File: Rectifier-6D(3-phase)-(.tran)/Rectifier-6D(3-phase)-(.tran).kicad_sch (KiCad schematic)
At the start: 11 parts

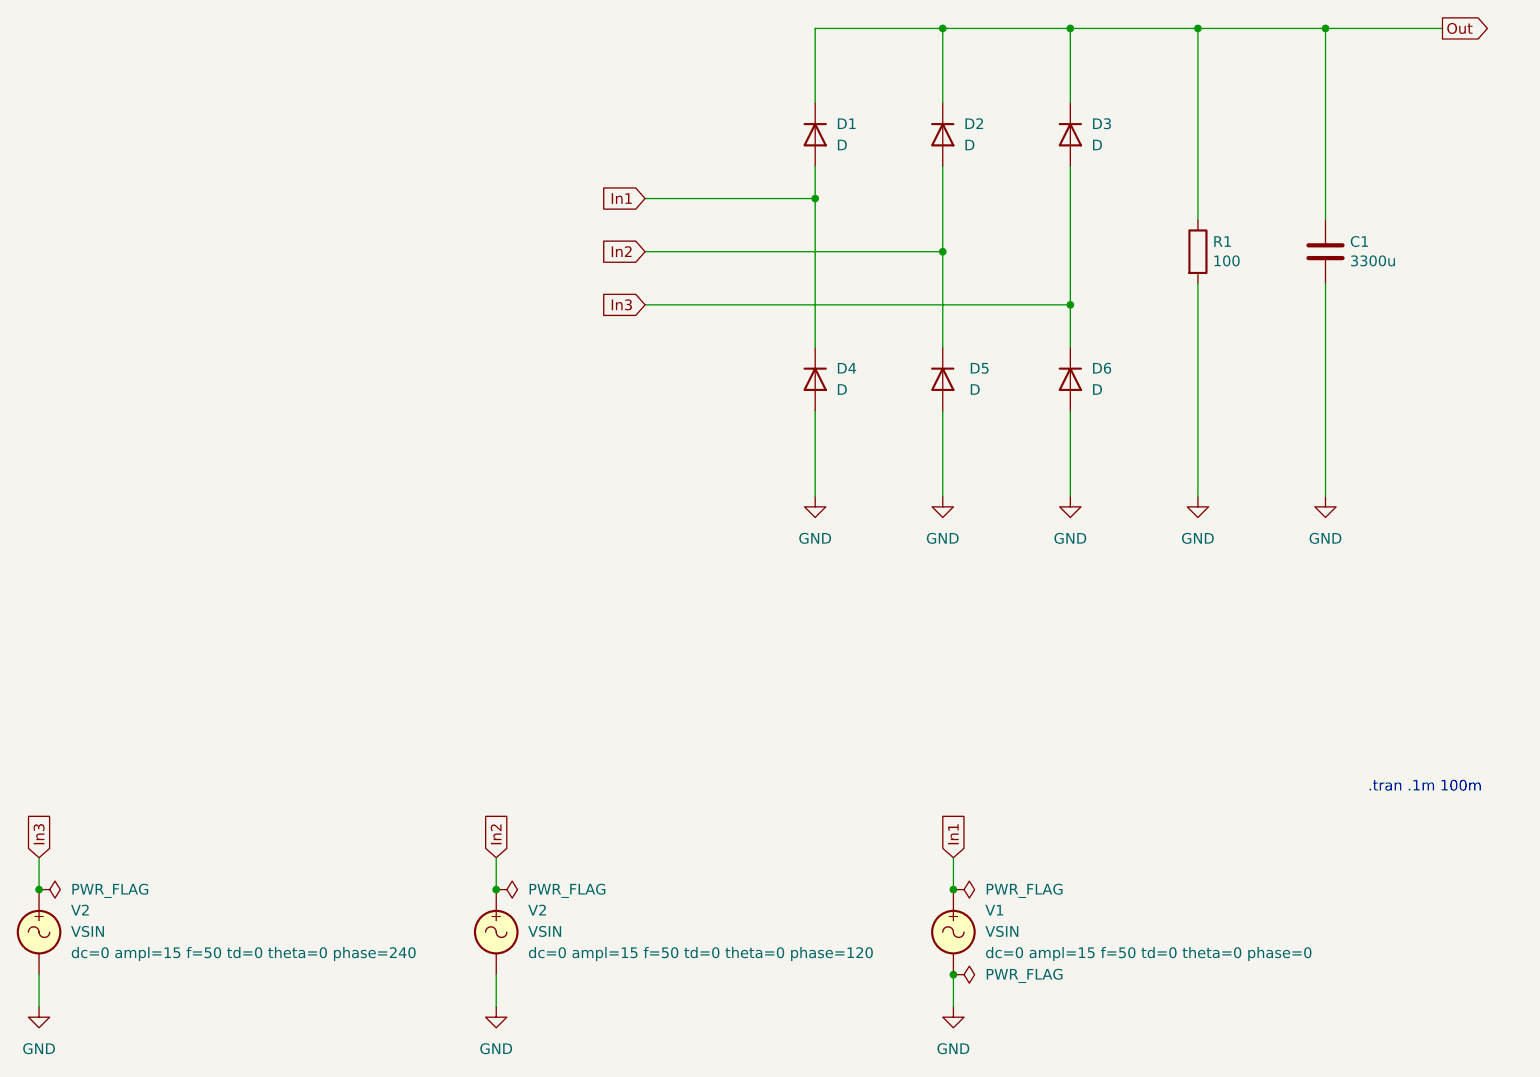
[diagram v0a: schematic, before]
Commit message: Updated all schematics and prepared for KiCad 8.0
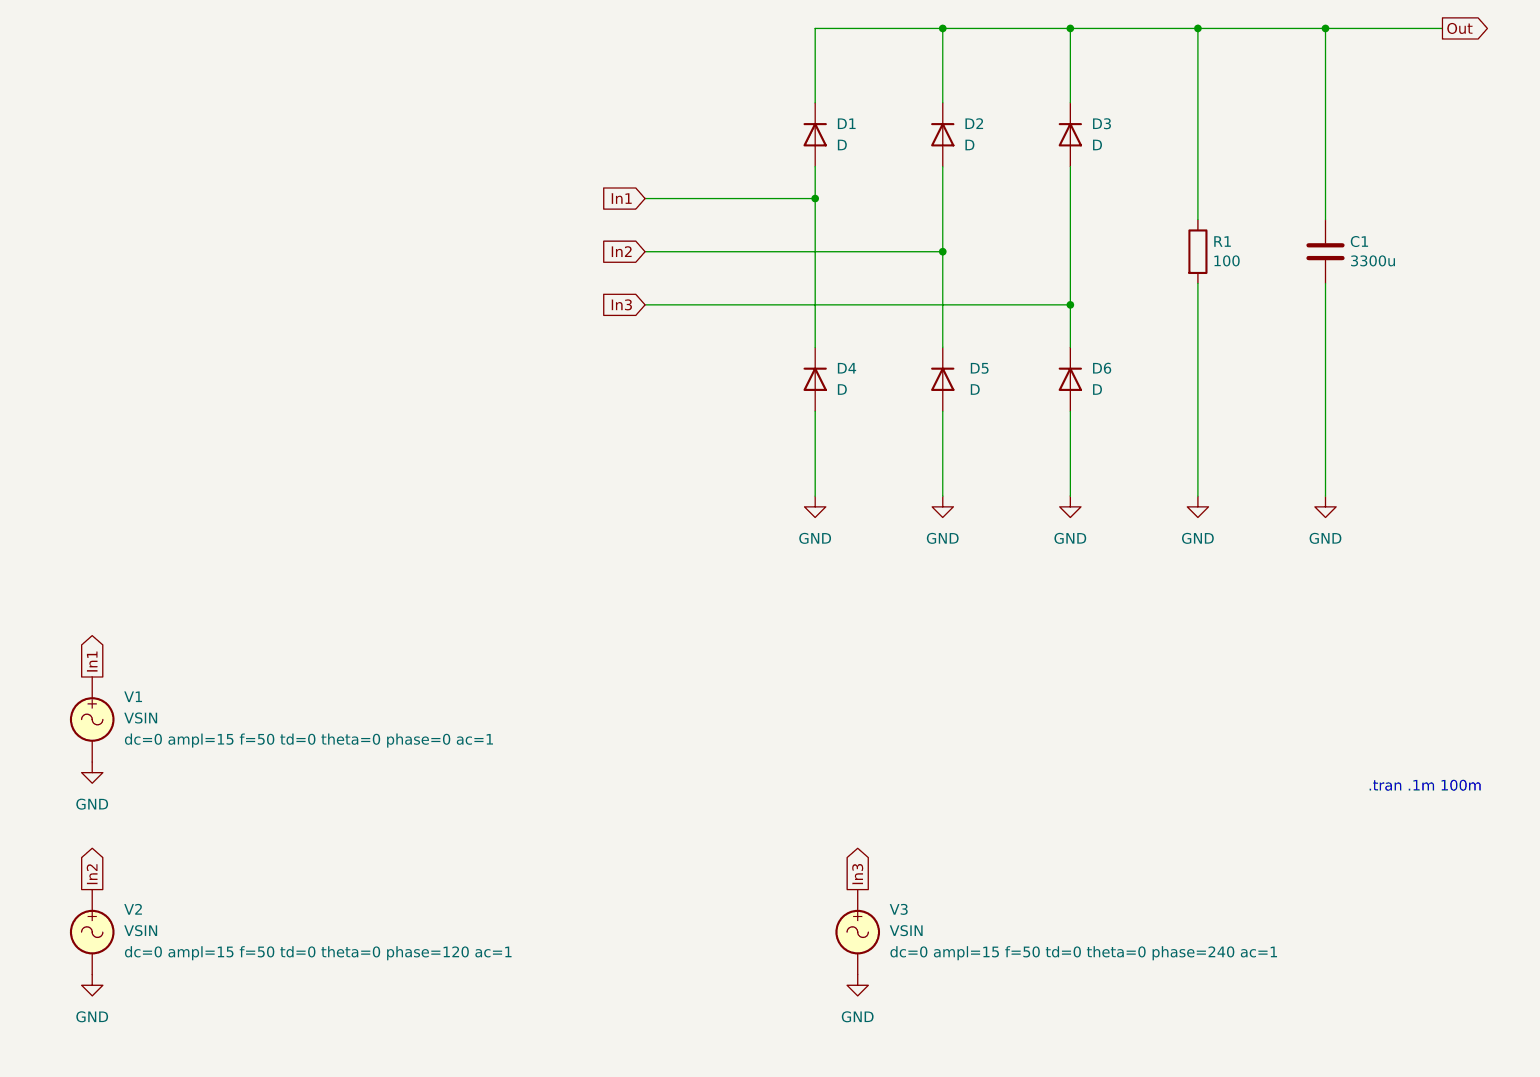
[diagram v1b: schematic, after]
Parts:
- removed V2 (x2): VSIN, symbol Simulation_SPICE:VSIN
- added V2, V3: VSIN, symbol Simulation_SPICE:VSIN
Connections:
- net GND: now also V2.2, V3.2
- net In2: now also V2.1
- net In3: now also V3.1
